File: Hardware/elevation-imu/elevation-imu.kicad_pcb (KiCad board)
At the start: 2 copper layers, 39.5 x 16 mm, 26 parts, among them J1 Conn_02x04_Odd_Even, Q1 BSS138, Q2 BSS138, Q3 BSS138, U1 LSM6DSO32, U2 74HCT541, U3 TC2015-3.3VxCTTR

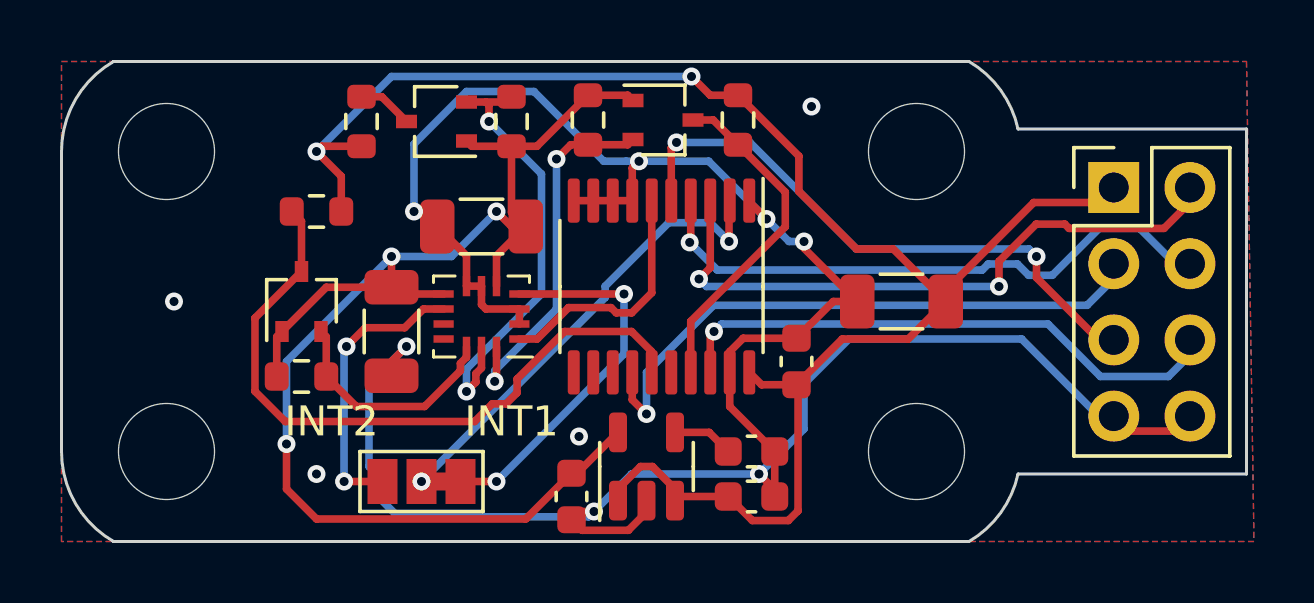
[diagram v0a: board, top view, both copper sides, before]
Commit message: EIMU: Fix disconnected SCL
This commit fixes a mistake where SCL and SCK were not connected.
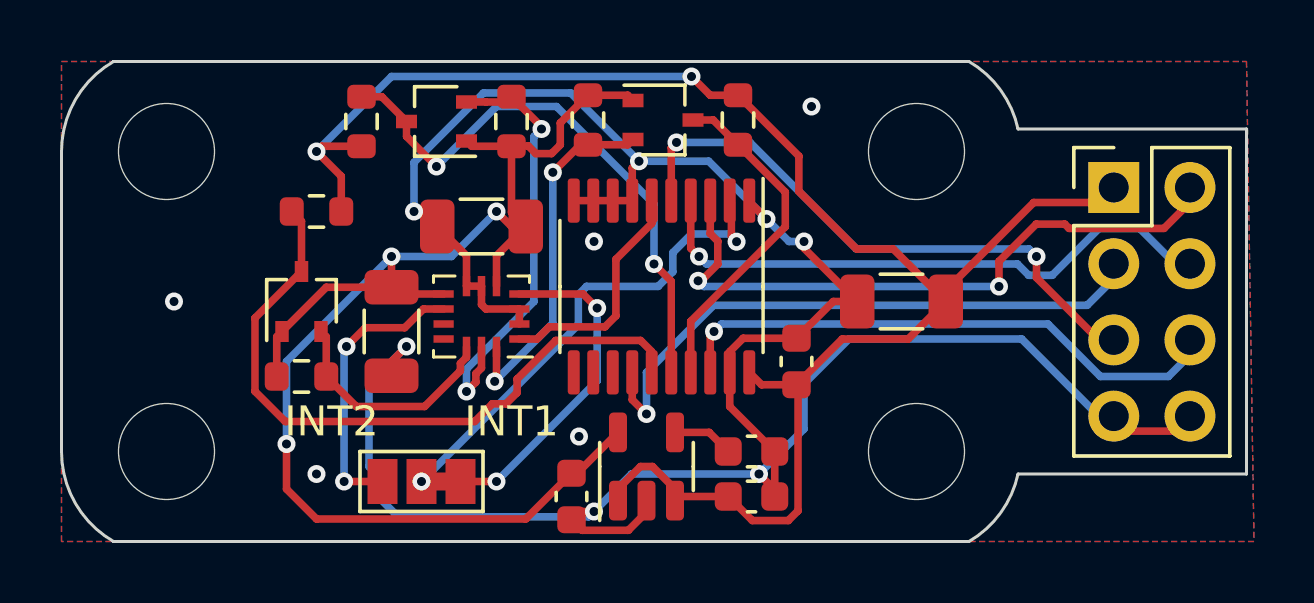
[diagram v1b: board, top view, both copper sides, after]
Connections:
- Q2 pad 3: /SCL_HV -> /CLK_HV
- R4 pad 2: /SCL_HV -> /CLK_HV
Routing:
- net /CLK_HV: track 0.00 -> 19.0 mm, vias 0 -> 2
- net /SCL_HV: track 1.84 -> 0.00 mm
- net Net-(JP1-Pad1): track 12.7 -> 11.2 mm
- net /INT: track 15.7 -> 16.5 mm
- net +3V3: track 47.5 -> 48.2 mm
- net GND: track 85.6 -> 85.2 mm, vias 11 -> 12

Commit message: Add intereferometer radio hardware
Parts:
- added TP1: TestPoint, TestPoint:TestPoint_THTPad_D1.0mm_Drill0.5mm, F.Cu at (110.4, 116.8)
- added TP2: TestPoint, TestPoint:TestPoint_THTPad_D1.0mm_Drill0.5mm, F.Cu at (138.2, 112.0)
- added TP3: TestPoint, TestPoint:TestPoint_THTPad_D1.0mm_Drill0.5mm, F.Cu at (106.0, 115.0)
- added TP4: TestPoint, TestPoint:TestPoint_THTPad_D1.0mm_Drill0.5mm, F.Cu at (138.2, 114.2)
- added TP5: TestPoint, TestPoint:TestPoint_THTPad_D1.0mm_Drill0.5mm, F.Cu at (108.8, 115.6)
- added TP6: TestPoint, TestPoint:TestPoint_THTPad_D1.0mm_Drill0.5mm, F.Cu at (138.2, 116.4)
- added TP7: TestPoint, TestPoint:TestPoint_THTPad_D1.0mm_Drill0.5mm, F.Cu at (137.6, 118.6)
- added TP8: TestPoint, TestPoint:TestPoint_THTPad_D1.0mm_Drill0.5mm, F.Cu at (138.0, 120.6)
- added TP9: TestPoint, TestPoint:TestPoint_THTPad_D1.0mm_Drill0.5mm, F.Cu at (107.0, 116.8)
- J1: footprint Connector_PinHeader_2.54mm:PinHeader_2x04_P2.54mm_Vertical -> MyParts:RJ45-UPDOWN_P100MIL
- moved J1 5.77 mm to (144.4, 116.0)
- moved Q2 1.60 mm to (115.9, 110.0)
- moved R3 1.60 mm to (118.4, 110.0)
- moved R4 1.60 mm to (113.4, 110.0)
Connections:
- J1 pad 3: /SDO_OUT -> /INT_OUT
- J1 pad 4: /CLK_IN -> /~{CS}_IN
- J1 pad 5: /~{CS}_IN -> GND
- J1 pad 6: /INT_OUT -> /CLK_IN
- J1 pad 8: GND -> /SDO_OUT
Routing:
- net /SDO: track 7.87 -> 32.3 mm, vias 0 -> 1
- net /SCL: track 14.5 -> 30.0 mm
- net /SDI: track 12.1 -> 24.8 mm
- net GND: track 85.2 -> 93.7 mm, vias 12 -> 15
- net +3V3: track 48.2 -> 40.7 mm
- net /~{CS}: track 7.83 -> 14.2 mm, vias 0 -> 1
- net /~{CS}_HV: track 22.6 -> 27.1 mm
- net /SDO_OUT: track 19.8 -> 23.4 mm
- net /SDI_IN: track 21.4 -> 18.9 mm, vias 2 -> 1
- net Net-(JP1-A): track 11.2 -> 12.9 mm
- net +5V: track 56.9 -> 58.4 mm
- net /CLK_HV: track 19.0 -> 20.3 mm
- net /CLK_IN: track 19.9 -> 18.9 mm
- net /INT: track 16.5 -> 17.4 mm
- net /~{CS}_IN: track 19.9 -> 20.9 mm, vias 2 -> 1
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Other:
- board text added: "CLK"
- board text added: "GND"
- board text added: "Hans Gaensbauer Eli Reed"
- board text added: "SCL"
- board text added: "SDI"
- board text added: "SDO"
- board text added: "~{CS}"
- board text removed: "Hans Gaensbauer and Eli Reed"
